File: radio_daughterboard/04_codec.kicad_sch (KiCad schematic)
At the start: 36 parts, among them J330 DNP radio audio codec probe, Q330 2N7002KT1G VHF PTT/suspend fa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, Q331 2N7002KT1G UHF PTT/suspend fa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, Q332 BSS84LT1G codec-loss force-mu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, U330 PCM2902CDBR USB audio codec, Y330 ABM8G-106-12.000MHZ-T 12MHz 1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

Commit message: Complete EC DFU port (J73) + DB power rework; verify schematic and board
- Add rear USB-C EC firmware programming port J73 (UFP/DFU) on Internal
  Services sheet: USBLC6-2P6 ESD (U63), 5.1k CC Rd resistors (R205/R211),
  22R series on D+/D- (R203/R204), mux-select hookup so BOOT0 high forces
  the USB mux to the DFU port
- Rename port ref J70->J73 after ham-radio collision; sync all net names
  (J73_CC1/J73_CC2)
- DB power rework: S5 gating + 3V3_STBY split, dual DCDC paths, GND
  returns on the standby rails; regenerate all sheets and re-verify
- sync_main_pcb_from_netlist: anchor placement for the 9 new footprints,
  scoped ECO support
- Board: rebuild main PCB with J73 footprint block (lib-sourced, net
  injection from netlist name attribute), sync pad nets for the 5 stale
  refs, remove duplicate R205/R211 copies
- Verified: check_schematic self-check OK (0 errors), radio DB contracts
  OK, ERC 0 errors, board DRC 0 electrical violations, board-vs-schematic
  net parity 0 conflicts, no duplicate refs
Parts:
- C330, C332, C333, C334, C335, C340, C341, C342, C343: MPN GRM21BR71A105KA01L -> (none); Manufacturer Murata -> (none)
- C331, C337: MPN GRM31CR71E106KA12L -> (none); Manufacturer Murata -> (none)
- C338, C339: MPN GRM1885C1H180JA01D -> (none); Manufacturer Murata -> (none)
- R330, R331: MPN RC0603FR-0722RL -> (none); Manufacturer Yageo -> (none)
- R334, R335: MPN RC0603FR-0782KL -> (none); Manufacturer Yageo -> (none)
- R336, R341: MPN RC0603FR-071KL -> (none); Manufacturer Yageo -> (none)
- R337: MPN RC0603FR-072R2L -> (none); Manufacturer Yageo -> (none)
- R338: MPN RC0603FR-071K5L -> (none); Manufacturer Yageo -> (none)
- R340: MPN RC0603FR-071ML -> (none); Manufacturer Yageo -> (none)
- R342, R343, R344, R345: MPN RC0603FR-07100KL -> (none); Manufacturer Yageo -> (none)

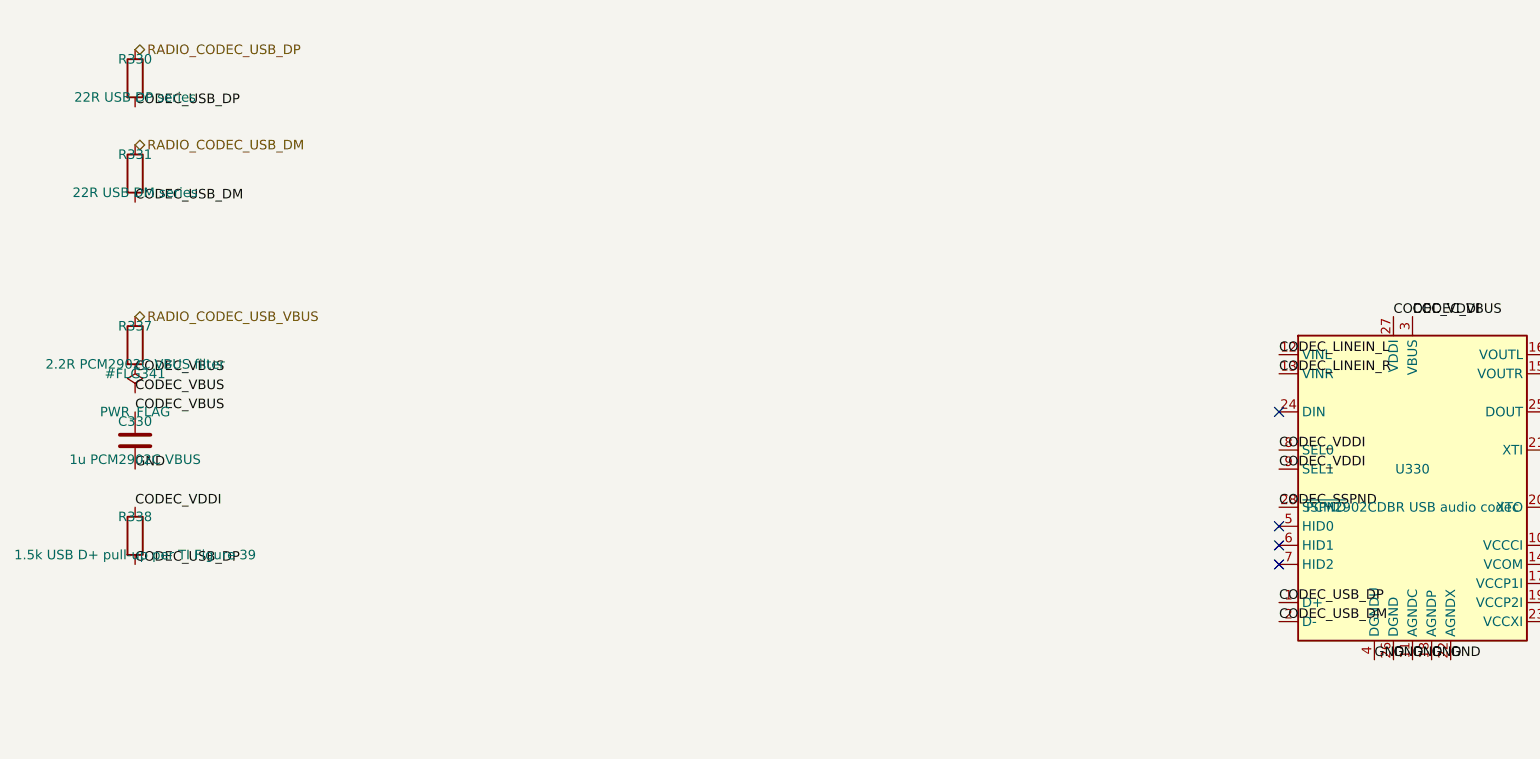
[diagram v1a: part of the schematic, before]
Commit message: get the main boards ready for routing
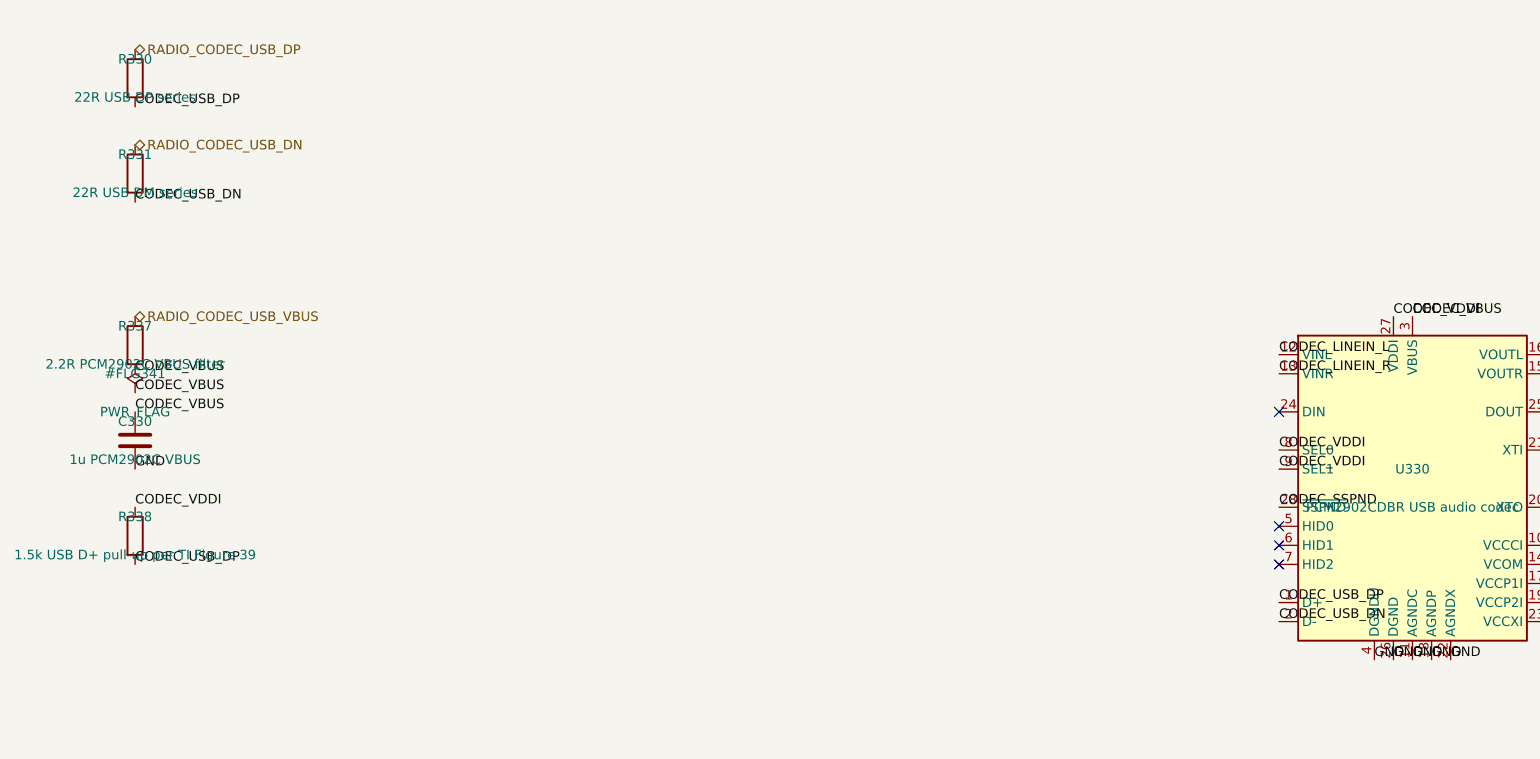
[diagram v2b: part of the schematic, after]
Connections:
- net CODEC_USB_DM renamed CODEC_USB_DN
- net RADIO_CODEC_USB_DM renamed RADIO_CODEC_USB_DN
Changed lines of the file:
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@@
   (effects (font (size 1.27 1.27)) (justify left bottom))
 )
-(label "CODEC_USB_DM"
+(label "CODEC_USB_DN"
   (at 172.72 162.56 0)
   (effects (font (size 1.27 1.27)) (justify left bottom))
@@
   )
 )
-(hierarchical_label "RADIO_CODEC_USB_DM"
+(hierarchical_label "RADIO_CODEC_USB_DN"
   (shape bidirectional)
   (at 20.32 99.06 0)
   (effects (font (size 1.27 1.27)) (justify left bottom))
 )
-(label "CODEC_USB_DM"
+(label "CODEC_USB_DN"
   (at 20.32 106.68 0)
   (effects (font (size 1.27 1.27)) (justify left bottom))
